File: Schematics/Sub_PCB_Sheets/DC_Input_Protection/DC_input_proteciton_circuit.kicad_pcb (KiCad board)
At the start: 2 copper layers, 68.5 x 44.5 mm, 23 parts, among them J1 CONN_66.9040-21_MTC, J2 CONN_66.9040-21_MTC, J23 464369202, J24 43650-0418, Q8 STB10NK60ZT4

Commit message: Milestone Finished WIP PCB for 7 PCBs, Set up folders for each PCB
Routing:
- net GND: track 33.6 -> 22.9 mm

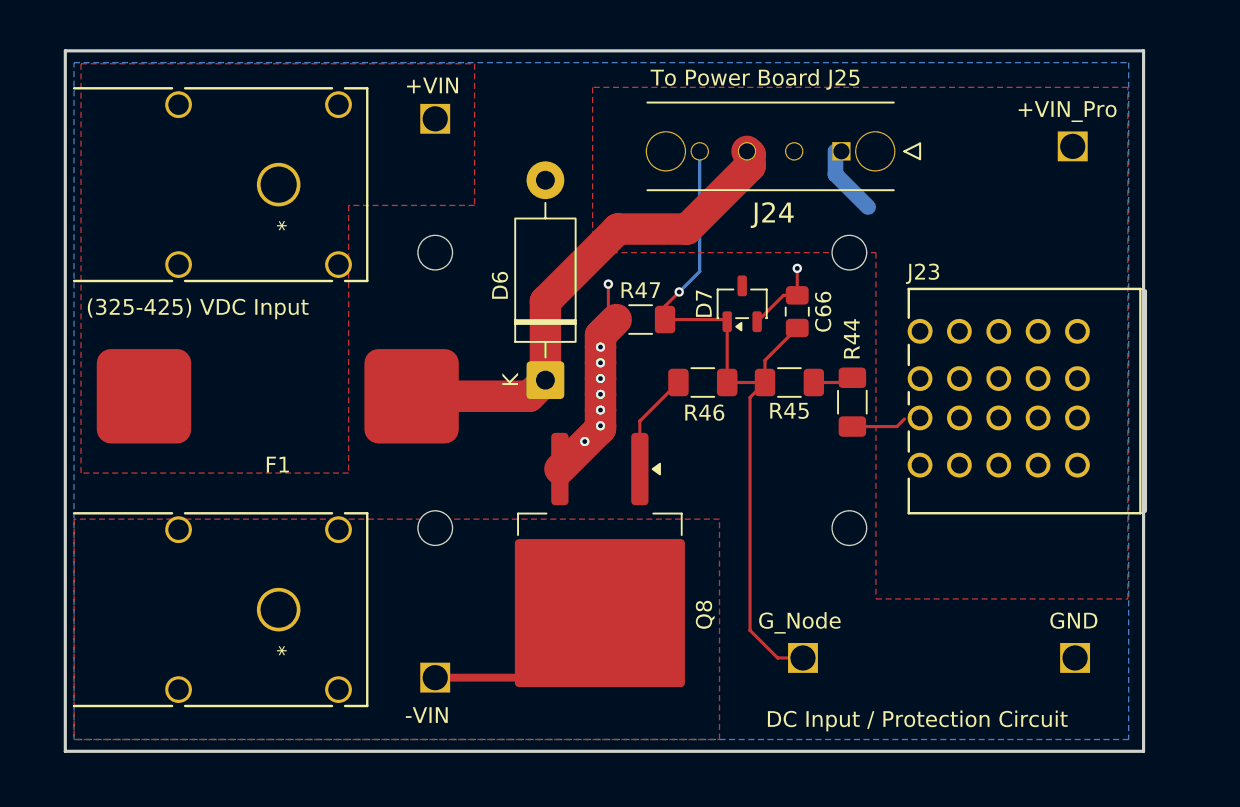
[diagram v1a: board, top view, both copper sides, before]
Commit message: Finishing DC Input PCB circuit and Fab Outputs
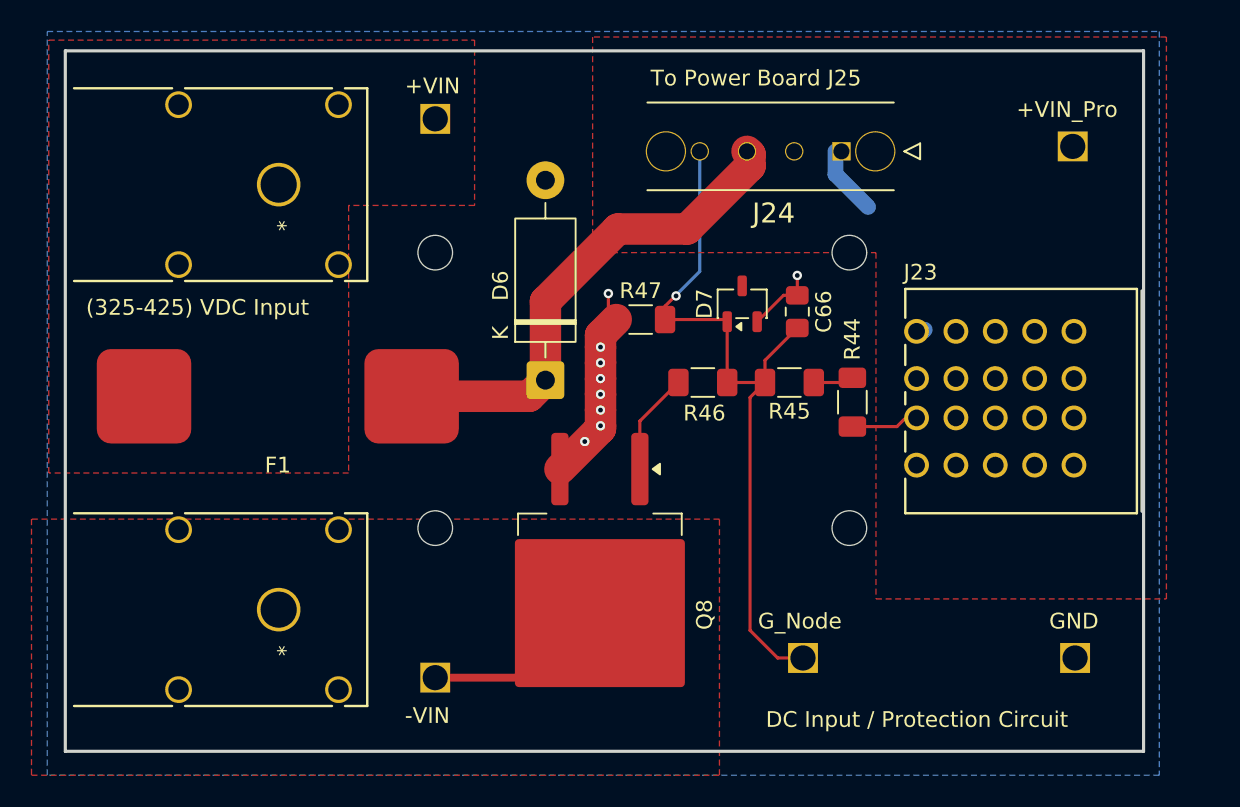
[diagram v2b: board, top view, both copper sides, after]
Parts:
- moved J23 0.22 mm to (216.9, 148.8)
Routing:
- net GND: track 22.9 -> 21.9 mm
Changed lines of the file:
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@@
 		)
 		(fp_text user "K"
-			(at 0 -2.2 90)
+			(at 3 -2.85 90)
 			(layer "F.SilkS")
 			(effects
@@
 	(footprint "SiC_Inverter:46436-900_02"
 		(layer "F.Cu")
-		(at 217.15 148.750001 90)
+		(at 216.9275 148.750001 90)
 		(tags "464369202 ")
 		(property "Reference" "J23"
@@
 	(gr_text "+VIN\n"
 		(at 174.415477 125.25 0)
-		(layer "F.SilkS" knockout)
+		(layer "F.SilkS")
 		(effects
 			(font
@@
 	(gr_text "-VIN\n"
 		(at 174.415477 165.25 0)
-		(layer "F.SilkS" knockout)
+		(layer "F.SilkS")
 		(effects
 			(font
@@
 	(gr_text "G_Node"
 		(at 196.85 159.25 0)
-		(layer "F.SilkS" knockout)
+		(layer "F.SilkS")
 		(effects
 			(font
@@
 	(gr_text "+VIN_Pro"
 		(at 213.272619 126.75 0)
-		(layer "F.SilkS" knockout)
+		(layer "F.SilkS")
 		(effects
 			(font
@@
 	(gr_text "GND\n"
 		(at 215.35 159.25 0)
-		(layer "F.SilkS" knockout)
+		(layer "F.SilkS")
 		(effects
 			(font
@@
 	)
 	(segment
-		(start 199.35 136.25)
-		(end 199.35 137.9625)
-		(width 0.2)
+		(start 186.85 146.25)
+		(end 186.85 145.25)
+		(width 2)
 		(layer "F.Cu")
 		(net "GND")
 	)
 	(segment
-		(start 186.85 146.25)
-		(end 186.85 145.25)
-		(width 2)
+		(start 199.35 136.7)
+		(end 199.35 137.9625)
+		(width 0.2)
 		(layer "F.Cu")
 		(net "GND")
@@
 	)
 	(segment
-		(start 187.35 137.25)
-		(end 187.35 139)
-		(width 0.2)
+		(start 186.85 140.5)
+		(end 187.85 139.5)
+		(width 2)
 		(layer "F.Cu")
 		(net "GND")
 	)
 	(segment
-		(start 186.85 140.5)
-		(end 187.85 139.5)
-		(width 2)
+		(start 187.35 137.85)
+		(end 187.35 139)
+		(width 0.2)
 		(layer "F.Cu")
 		(net "GND")
@@
 	)
 	(via
-		(at 199.35 136.25)
+		(at 199.35 136.7)
 		(size 0.6)
 		(drill 0.3)
@@
 	)
 	(via
-		(at 187.35 137.25)
+		(at 187.35 137.85)
 		(size 0.6)
 		(drill 0.3)
@@
 	)
 	(segment
+		(start 190.95 138.65)
+		(end 190.95 139.5)
+		(width 0.2)
+		(layer "F.Cu")
+		(net "/Con_Pro_Gate_node_output")
+	)
+	(segment
+		(start 191.65 138)
+		(end 191.6 138)
+		(width 0.2)
+		(layer "F.Cu")
+		(net "/Con_Pro_Gate_node_output")
+	)
+	(segment
 		(start 190.95 139.5)
 		(end 194.7625 139.5)
@@
 	)
 	(segment
+		(start 191.6 138)
+		(end 190.95 138.65)
+		(width 0.2)
+		(layer "F.Cu")
+		(net "/Con_Pro_Gate_node_output")
+	)
+	(segment
 		(start 194.9 139.6375)
 		(end 194.9 143.5)
@@
 	)
 	(segment
-		(start 190.95 139.5)
-		(end 190.95 138.65)
-		(width 0.2)
-		(layer "F.Cu")
-		(net "/Con_Pro_Gate_node_output")
-	)
-	(segment
 		(start 198.1 161)
 		(end 196.35 159.25)
@@
 	)
 	(segment
-		(start 190.95 138.65)
-		(end 191.85 137.75)
-		(width 0.2)
-		(layer "F.Cu")
-		(net "/Con_Pro_Gate_node_output")
-	)
-	(segment
 		(start 196.35 144.45)
 		(end 197.3 143.5)
@@
 	)
 	(via
-		(at 191.85 137.75)
+		(at 191.65 138)
 		(size 0.6)
 		(drill 0.3)
@@
 	)
 	(segment
-		(start 191.85 137.75)
+		(start 191.65 138)
+		(end 191.65 137.95)
+		(width 0.2)
+		(layer "B.Cu")
+		(net "/Con_Pro_Gate_node_output")
+	)
+	(segment
+		(start 191.65 137.95)
 		(end 193.15535 136.44465)
 		(width 0.2)
@@
 		(polygon
 			(pts
-				(xy 153.85 123.25) (xy 178.85 123.25) (xy 178.85 132.25) (xy 170.85 132.25) (xy 170.85 149.25) (xy 153.85 149.25)
+				(xy 151.8 121.75) (xy 178.85 121.75) (xy 178.85 132.25) (xy 170.85 132.25) (xy 170.85 149.25) (xy 151.8 149.25)
 			)
 		)
@@
 		(polygon
 			(pts
-				(xy 186.35 124.75) (xy 186.35 135.25) (xy 204.35 135.25) (xy 204.35 157.25) (xy 220.35 157.25) (xy 220.35 124.75)
+				(xy 186.35 121.55) (xy 186.35 135.25) (xy 204.35 135.25) (xy 204.35 157.25) (xy 222.8 157.25) (xy 222.8 121.55)
 			)
 		)
@@
 		(polygon
 			(pts
-				(xy 153.406684 152.180001) (xy 153.406684 166.180001) (xy 194.406684 166.180001) (xy 194.406684 152.180001)
+				(xy 150.7 152.180001) (xy 150.7 168.45) (xy 194.406684 168.45) (xy 194.406684 152.180001)
 			)
 		)
@@
 		(polygon
 			(pts
-				(xy 153.406684 123.180001) (xy 220.406684 123.180001) (xy 220.406684 166.180001) (xy 153.406684 166.180001)
+				(xy 151.7 121.2) (xy 222.35 121.2) (xy 222.35 168.45) (xy 151.7 168.45)
 			)
 		)
